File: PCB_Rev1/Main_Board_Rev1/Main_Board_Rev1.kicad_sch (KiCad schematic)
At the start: 1 part, among them J1 Raspberry_Pi_2_3

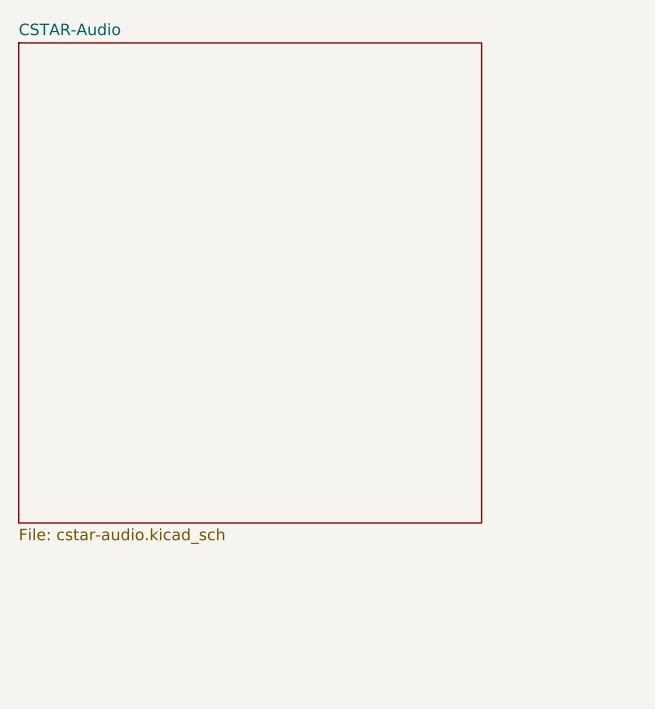
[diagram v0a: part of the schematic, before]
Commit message: Audio schem file deleted
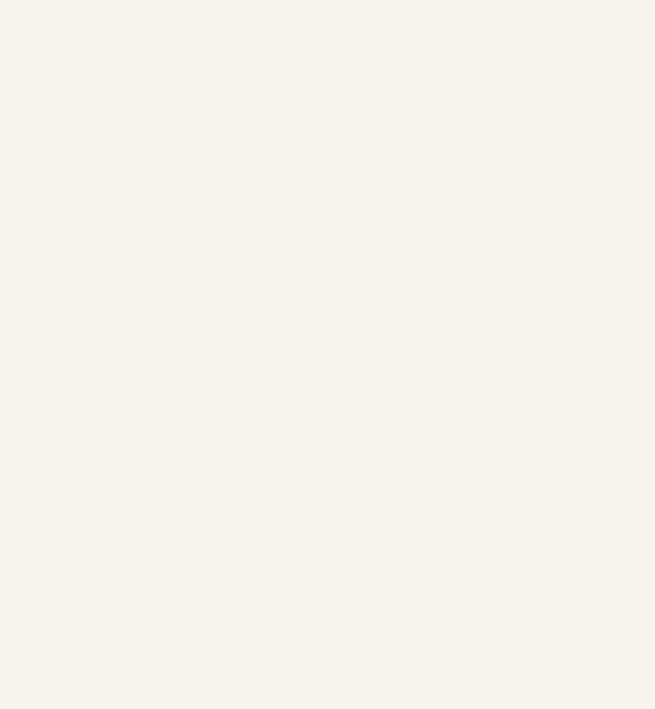
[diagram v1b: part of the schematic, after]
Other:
- removed sheet CSTAR-Audio
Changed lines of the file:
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@@
-	)
-	(sheet
-		(at 21.59 26.67)
-		(size 51.435 53.34)
-		(fields_autoplaced yes)
-		(stroke
-			(width 0.1524)
-			(type solid)
-		)
-		(fill
-			(color 0 0 0 0.0000)
-		)
-		(property "Sheetname" "CSTAR-Audio"
-			(at 21.59 25.9584 0)
-			(effects
-				(font
-					(size 1.27 1.27)
-				)
-				(justify left bottom)
-			)
-		)
-		(property "Sheetfile" "cstar-audio.kicad_sch"
-			(at 21.59 80.5946 0)
-			(effects
-				(font
-					(size 1.27 1.27)
-				)
-				(justify left top)
-			)
-		)
-		(instances
-			(project "Main_Board_Rev1"
-				(path "/8f5a23de-a1fa-4202-92fb-c2ac3de0338c"
-					(page "4")
-				)
-			)
-		)
 	)
 	(sheet

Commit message: Added new footprints
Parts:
- J1: footprint (none) -> Footprints:RPiConnector
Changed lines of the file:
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@@
 			)
 		)
-		(property "Footprint" ""
+		(property "Footprint" "Footprints:RPiConnector"
 			(at 140.97 64.77 0)
 			(effects

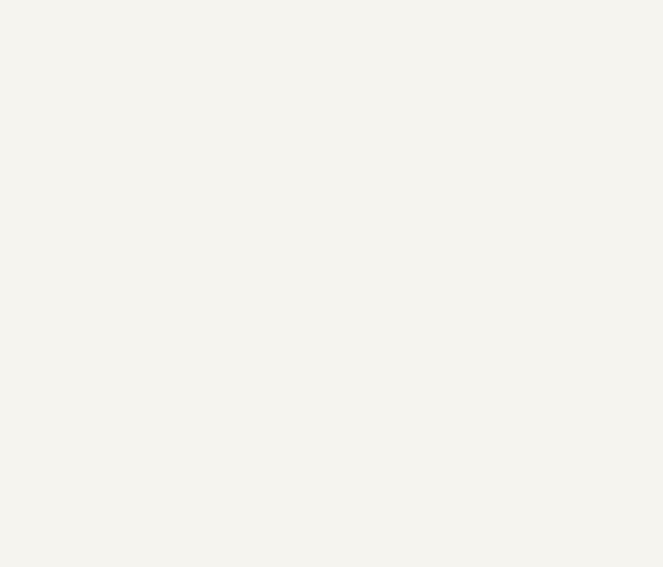
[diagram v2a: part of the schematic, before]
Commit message: Edge cuts complete (borders + holes)
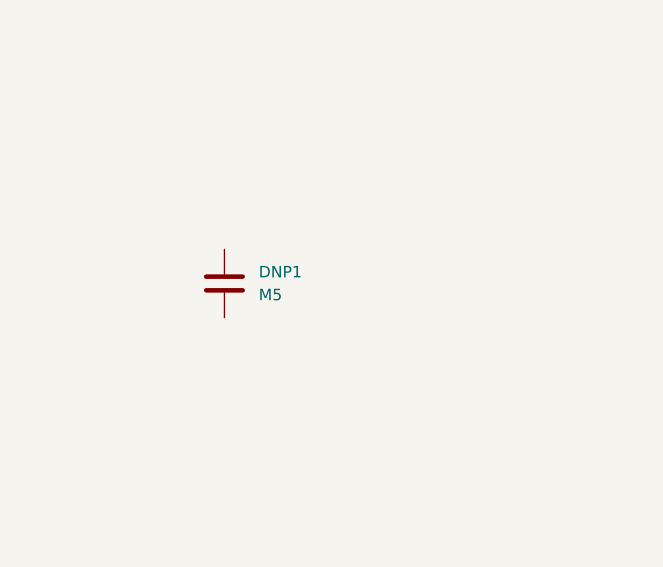
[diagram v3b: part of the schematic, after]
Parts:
- added DNP1: M5, MountingHole:MountingHole_5.3mm_M5, symbol Device:C
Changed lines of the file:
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@@
+		)
+	)
+	(symbol
+		(lib_id "Device:C")
+		(at 44.45 62.23 0)
+		(unit 1)
+		(exclude_from_sim no)
+		(in_bom yes)
+		(on_board yes)
+		(dnp no)
+		(fields_autoplaced yes)
+		(property "Reference" "DNP1"
+			(at 48.26 60.9599 0)
+			(effects
+				(font
+					(size 1.27 1.27)
+				)
+				(justify left)
+			)
+		)
+		(property "Value" "M5"
+			(at 48.26 63.4999 0)
+			(effects
+				(font
+					(size 1.27 1.27)
+				)
+				(justify left)
+			)
+		)
+		(property "Footprint" "MountingHole:MountingHole_5.3mm_M5"
+			(at 45.4152 66.04 0)
+			(effects
+				(font
+					(size 1.27 1.27)
+				)
+				(hide yes)
+			)
+		)
+		(property "Datasheet" "~"
+			(at 44.45 62.23 0)
+			(effects
+				(font
+					(size 1.27 1.27)
+				)
+				(hide yes)
+			)
+		)
+		(property "Description" "Unpolarized capacitor"
+			(at 44.45 62.23 0)
+			(effects
+				(font
+					(size 1.27 1.27)
+				)
+				(hide yes)
+			)
+		)
+		(pin "1"
+		)
+		(pin "2"
+		)
+		(instances
+			(project "Main_Board_Rev1"
+				(path "/8f5a23de-a1fa-4202-92fb-c2ac3de0338c"
+					(reference "DNP1")
+					(unit 1)
+				)
+			)
 		)
 	)

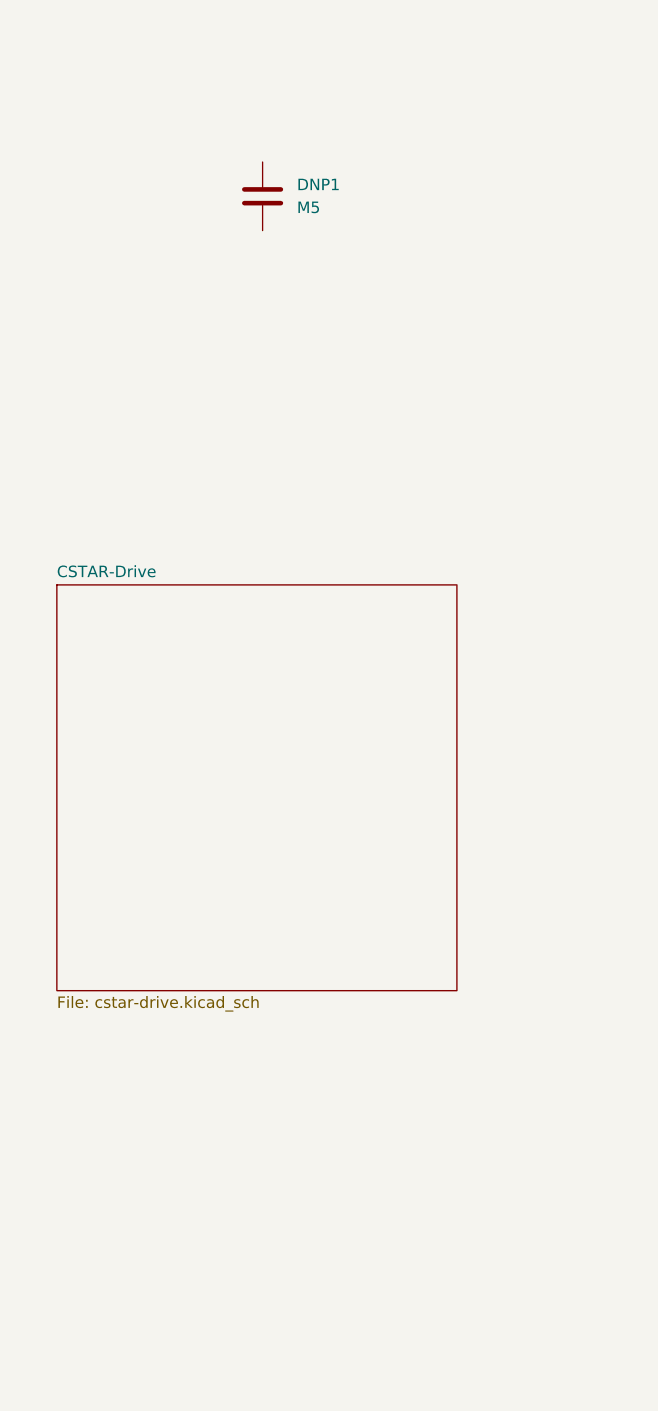
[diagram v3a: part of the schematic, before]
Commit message: mounting hole labeled
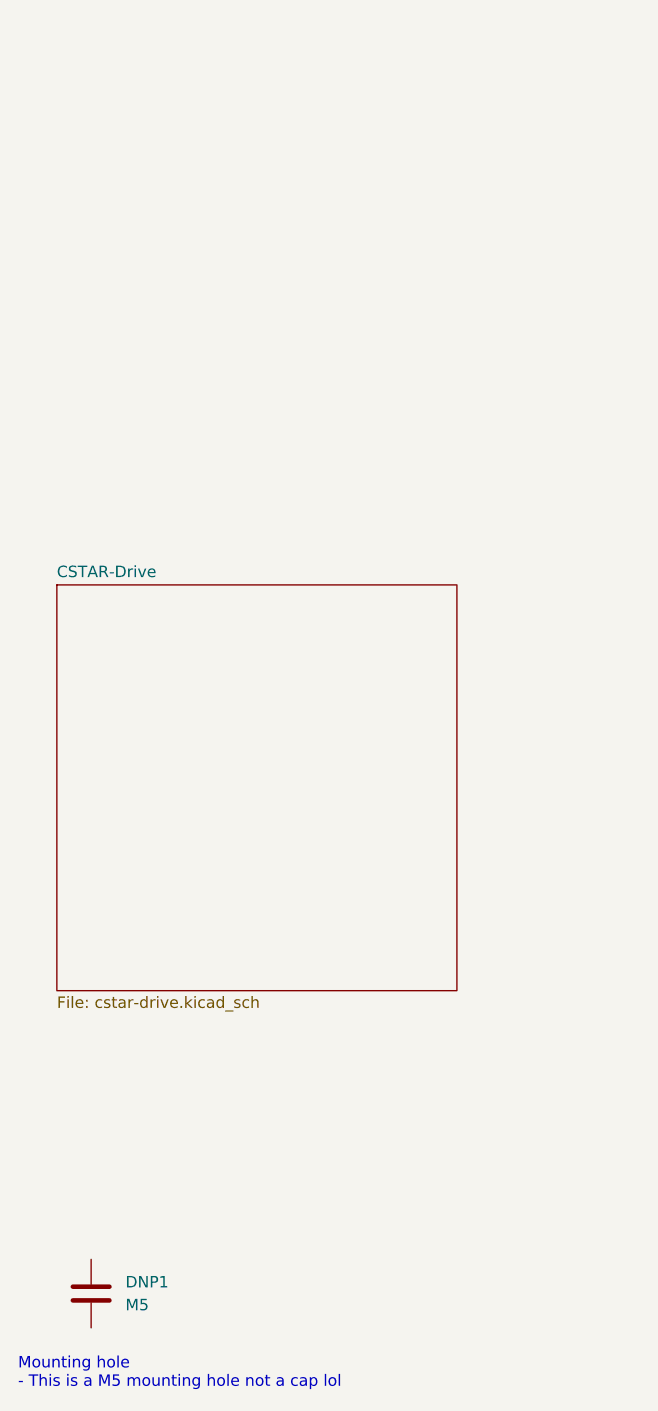
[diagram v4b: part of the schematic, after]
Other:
- note added: "Mounting hole - This is a M5 mounting hole not a cap lol"
- moved on the sheet: DNP1
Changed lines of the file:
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@@
 	(generator_version "8.0")
 	(paper "A4")
+	(text "Mounting hole\n- This is a M5 mounting hole not a cap lol\n"
+		(exclude_from_sim no)
+		(at 17.272 193.04 0)
+		(effects
+			(font
+				(size 1.27 1.27)
+			)
+			(justify left)
+		)
+	)
 	(text "Our MCU: RPi\n- Make sure the footprint for this component is designed for our exact model of RPi\n- RPi model 4B"
 		(exclude_from_sim no)
@@
 	(symbol
 		(lib_id "Device:C")
-		(at 44.45 62.23 0)
+		(at 25.4 184.15 0)
 		(unit 1)
 		(exclude_from_sim no)
@@
 		(fields_autoplaced yes)
 		(property "Reference" "DNP1"
-			(at 48.26 60.9599 0)
+			(at 29.21 182.8799 0)
 			(effects
 				(font
@@
 		)
 		(property "Value" "M5"
-			(at 48.26 63.4999 0)
+			(at 29.21 185.4199 0)
 			(effects
 				(font
@@
 		)
 		(property "Footprint" "MountingHole:MountingHole_5.3mm_M5"
-			(at 45.4152 66.04 0)
+			(at 26.3652 187.96 0)
 			(effects
 				(font
@@
 		)
 		(property "Datasheet" "~"
-			(at 44.45 62.23 0)
+			(at 25.4 184.15 0)
 			(effects
 				(font
@@
 		)
 		(property "Description" "Unpolarized capacitor"
-			(at 44.45 62.23 0)
-			(effects
-				(font
+			(at 25.4 184.15 0)
+			(effects
+				(font

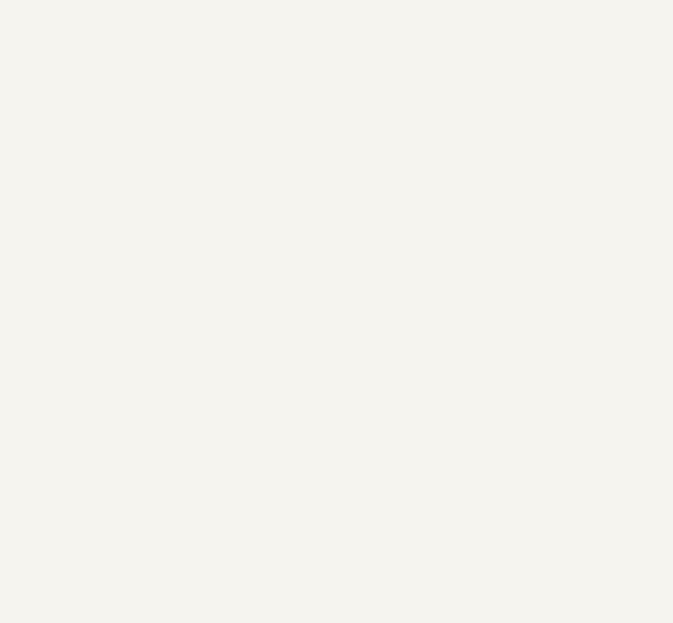
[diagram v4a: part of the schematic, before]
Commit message: Audio Subsystem Re-created
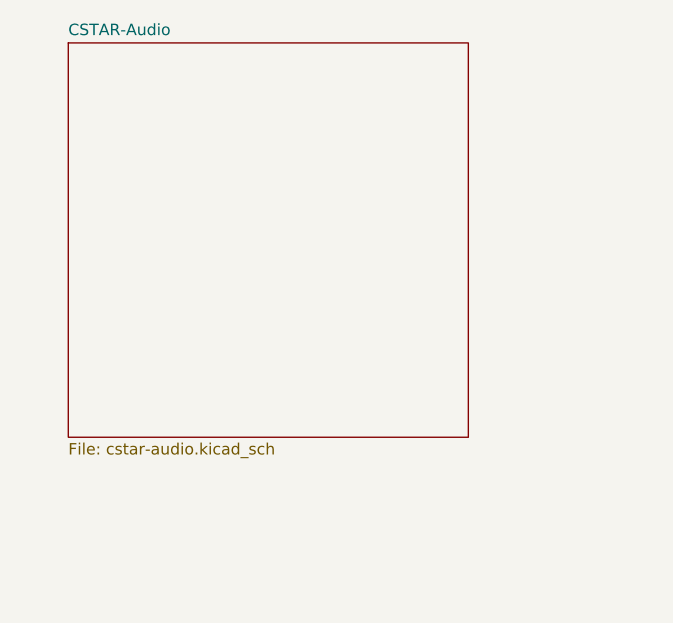
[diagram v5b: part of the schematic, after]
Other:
- added sheet CSTAR-Audio (cstar-audio.kicad_sch)
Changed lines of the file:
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@@
+		)
+	)
+	(sheet
+		(at 22.86 29.21)
+		(size 44.45 43.815)
+		(fields_autoplaced yes)
+		(stroke
+			(width 0.1524)
+			(type solid)
+		)
+		(fill
+			(color 0 0 0 0.0000)
+		)
+		(property "Sheetname" "CSTAR-Audio"
+			(at 22.86 28.4984 0)
+			(effects
+				(font
+					(size 1.27 1.27)
+				)
+				(justify left bottom)
+			)
+		)
+		(property "Sheetfile" "cstar-audio.kicad_sch"
+			(at 22.86 73.6096 0)
+			(effects
+				(font
+					(size 1.27 1.27)
+				)
+				(justify left top)
+			)
+		)
+		(instances
+			(project "Main_Board_Rev1"
+				(path "/8f5a23de-a1fa-4202-92fb-c2ac3de0338c"
+					(page "4")
+				)
+			)
 		)
 	)

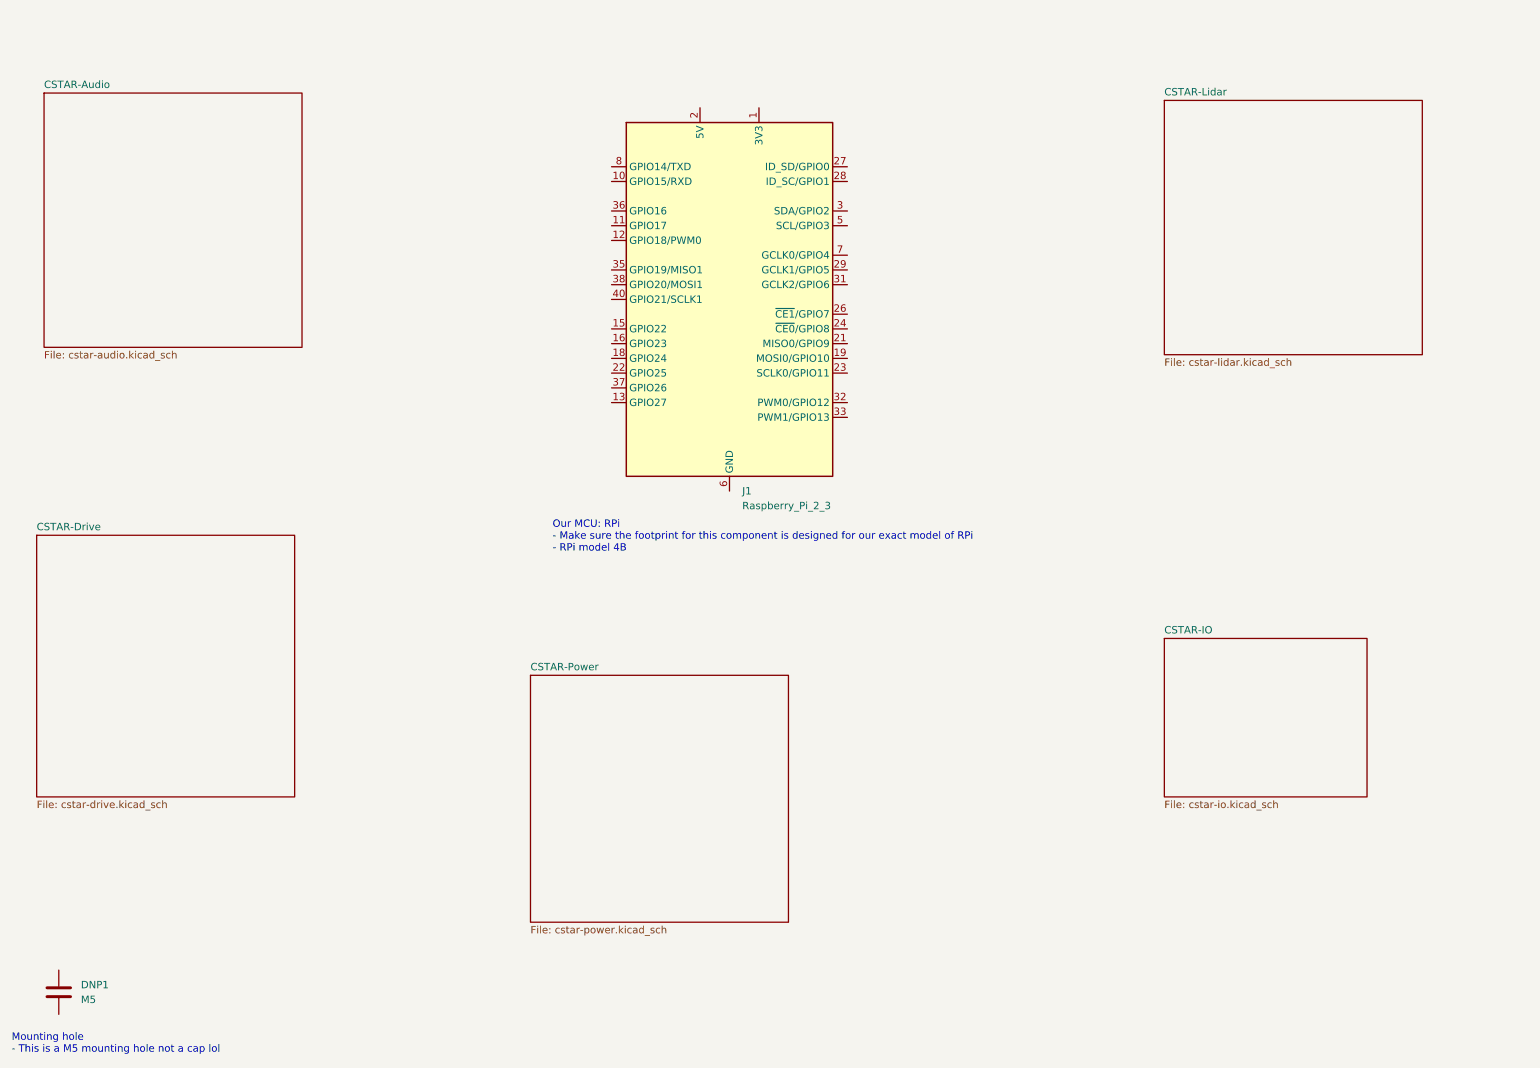
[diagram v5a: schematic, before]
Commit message: Connections to RPi GPIO Pins + Eliminating Errors from Layout
Global net connections made from RPi GPIO pins.
Error for mounting hole corrected -> mounting hole symbol imported into schematic and correct footprint assigned.
Warnings for J10, J11, J12 connectors resolved- imported footprint for the connector from online (error in the one imported from KiCAD libraries with pins S1 and S2 labeled as MP in the footprint)
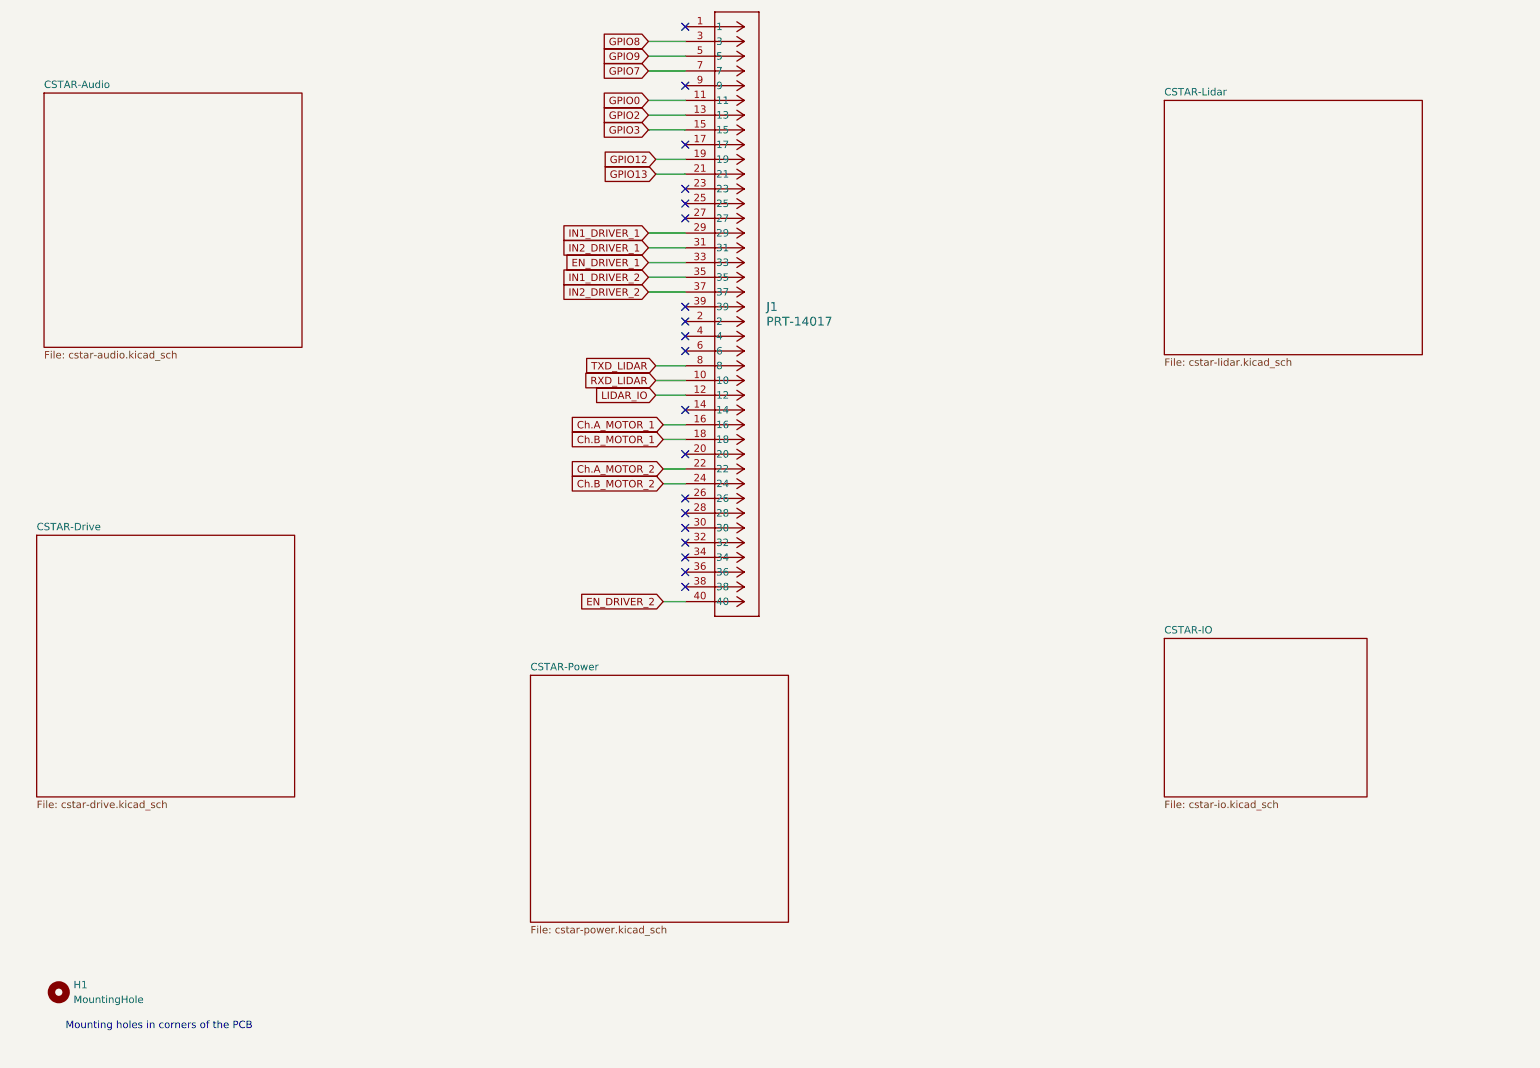
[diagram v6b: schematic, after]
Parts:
- removed DNP1: M5, MountingHole:MountingHole_5.3mm_M5, symbol Device:C
- removed J1: Raspberry_Pi_2_3, Footprints:RPiConnector, symbol Connector:Raspberry_Pi_2_3
- added H1: MountingHole, MountingHole:MountingHole_5.3mm_M5, symbol Mechanical:MountingHole
- added J1: PRT-14017, Footprints:RPiConnector, symbol RPiConnector:PRT-14017
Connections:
- new net Ch.A_MOTOR_1: J1.16
- new net Ch.A_MOTOR_2: J1.22
- new net Ch.B_MOTOR_1: J1.18
- new net Ch.B_MOTOR_2: J1.24
- new net EN_DRIVER_1: J1.33
- new net EN_DRIVER_2: J1.40
- new net GPIO0: J1.11
- new net GPIO12: J1.19
- new net GPIO13: J1.21
- new net GPIO2: J1.13
- new net GPIO3: J1.15
- new net GPIO7: J1.7
- new net GPIO8: J1.3
- new net GPIO9: J1.5
- new net IN1_DRIVER_1: J1.29
- new net IN1_DRIVER_2: J1.35
- new net IN2_DRIVER_1: J1.31
- new net IN2_DRIVER_2: J1.37
- new net LIDAR_IO: J1.12
- new net RXD_LIDAR: J1.10
- new net TXD_LIDAR: J1.8
- no-connect marks 0 -> 19
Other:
- note added: "Mounting holes in corners of the PCB"
- note removed: "Mounting hole - This is a M5 mounting hole not a cap lol"
- note removed: "Our MCU: RPi - Make sure the footprint for this component is designed for our exact model of RPi - RPi model 4B"
